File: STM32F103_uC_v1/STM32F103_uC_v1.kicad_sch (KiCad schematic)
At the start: 1 part

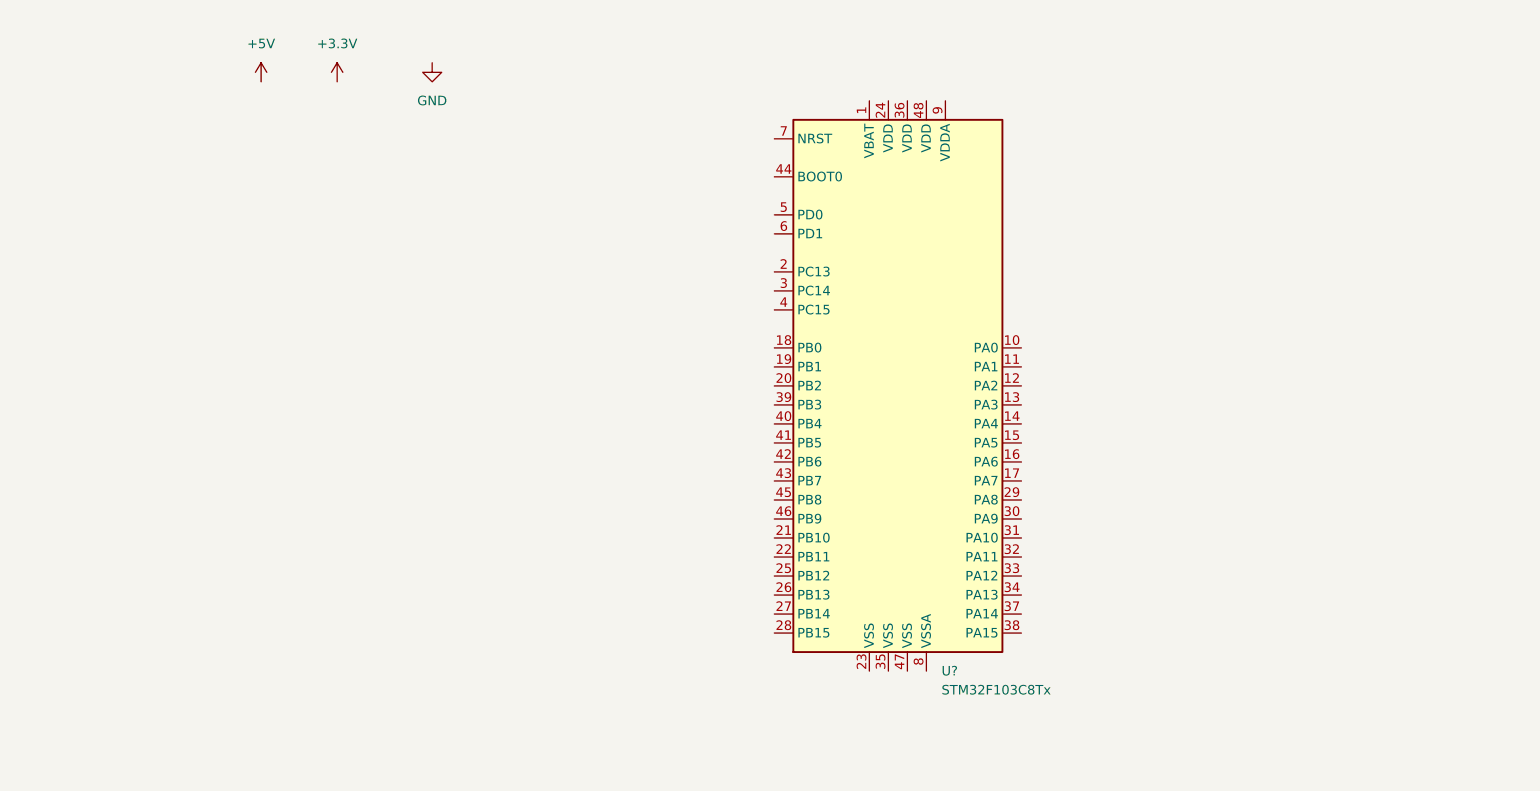
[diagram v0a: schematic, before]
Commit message: 100nF -> 10nF
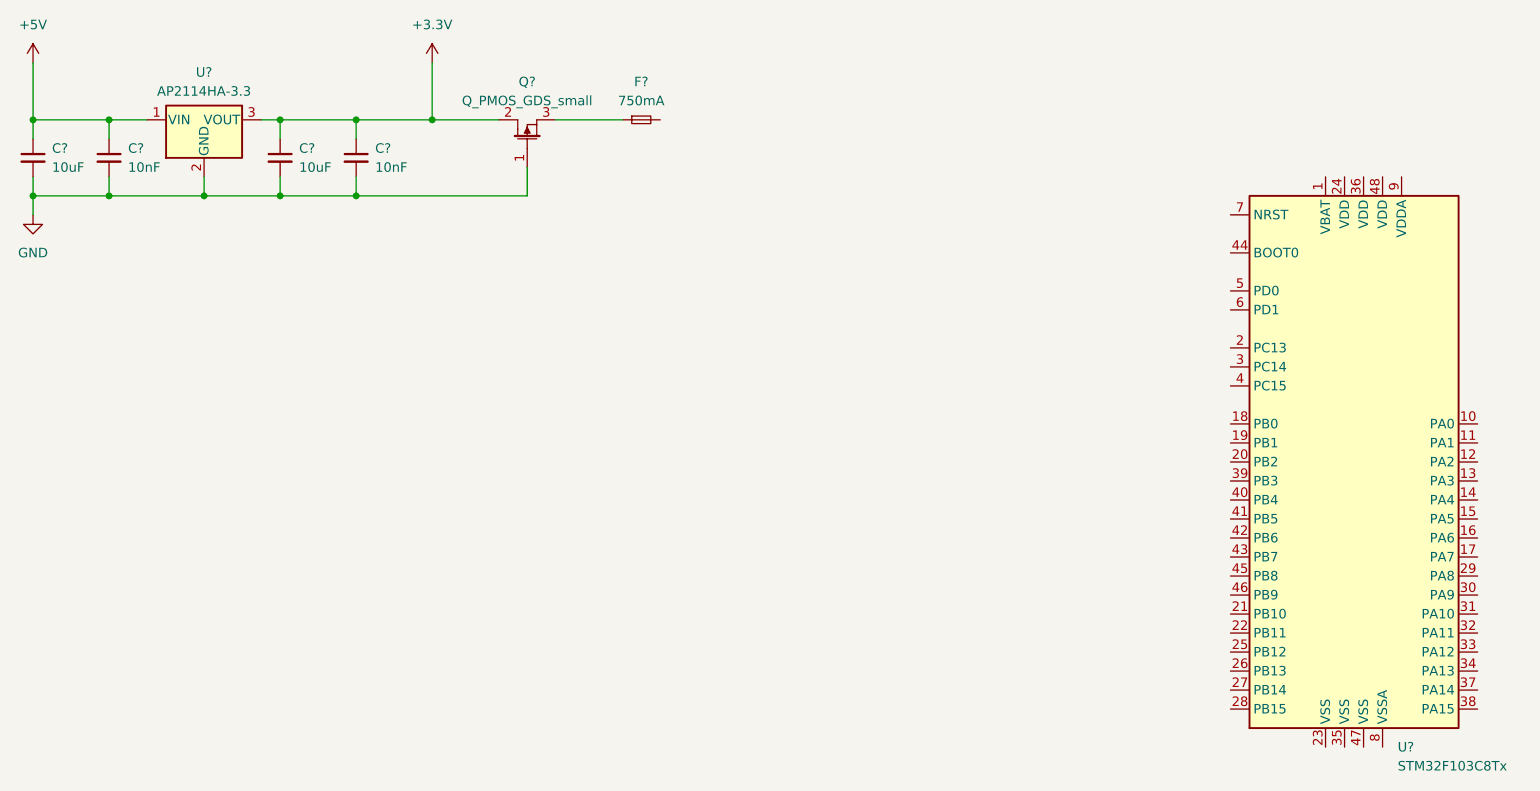
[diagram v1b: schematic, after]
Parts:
- added C? (x2): 10uF, symbol Device:C_Small
- added C? (x2): 10nF, symbol Device:C_Small
- added F?: 750mA, symbol Device:Fuse_Small
- added Q?: Q_PMOS_GDS_small, symbol STM32F103_uC:Q_PMOS_GDS_small
- added U?: AP2114HA-3.3, Package_TO_SOT_SMD:SOT-223-3_TabPin2, symbol STM32F103_uC:AP2114HA-3.3TRG1
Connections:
- net +3V3: now also C?.1, C?.1, Q?.2, U?.3 (VOUT)
- net +5V: now also C?.1, C?.1, U?.1 (VIN)
- net GND: now also C?.2, C?.2, C?.2, C?.2, Q?.1, U?.2 (GND)
- new net: F?.1, Q?.3
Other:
- moved on the sheet: U?

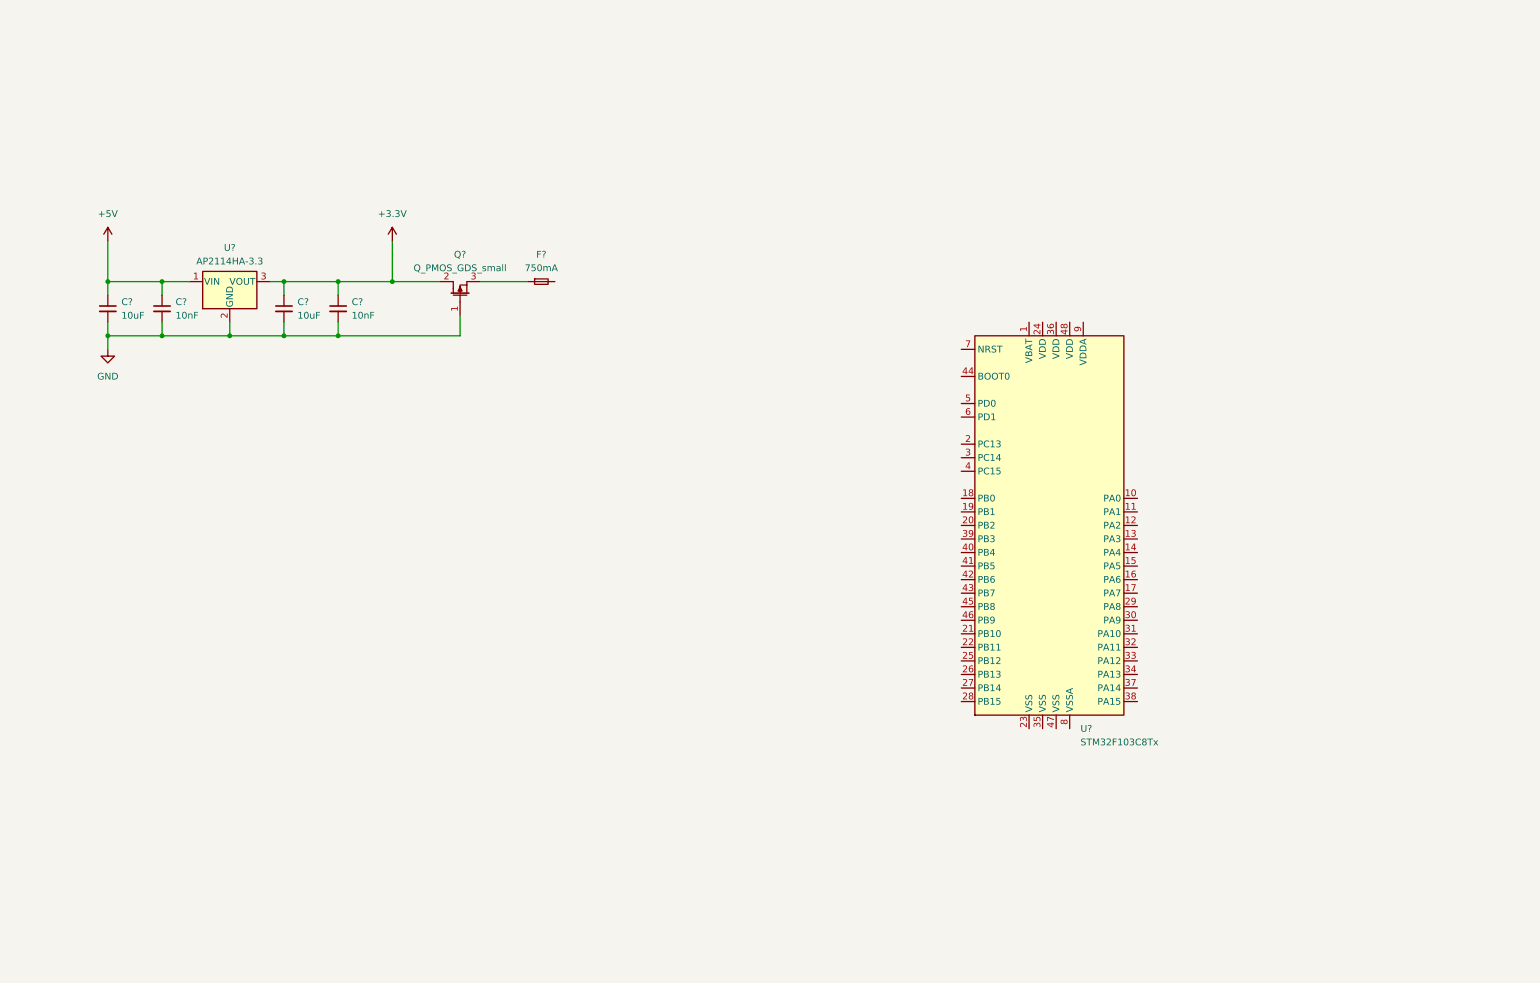
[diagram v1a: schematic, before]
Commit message: Schematic additions
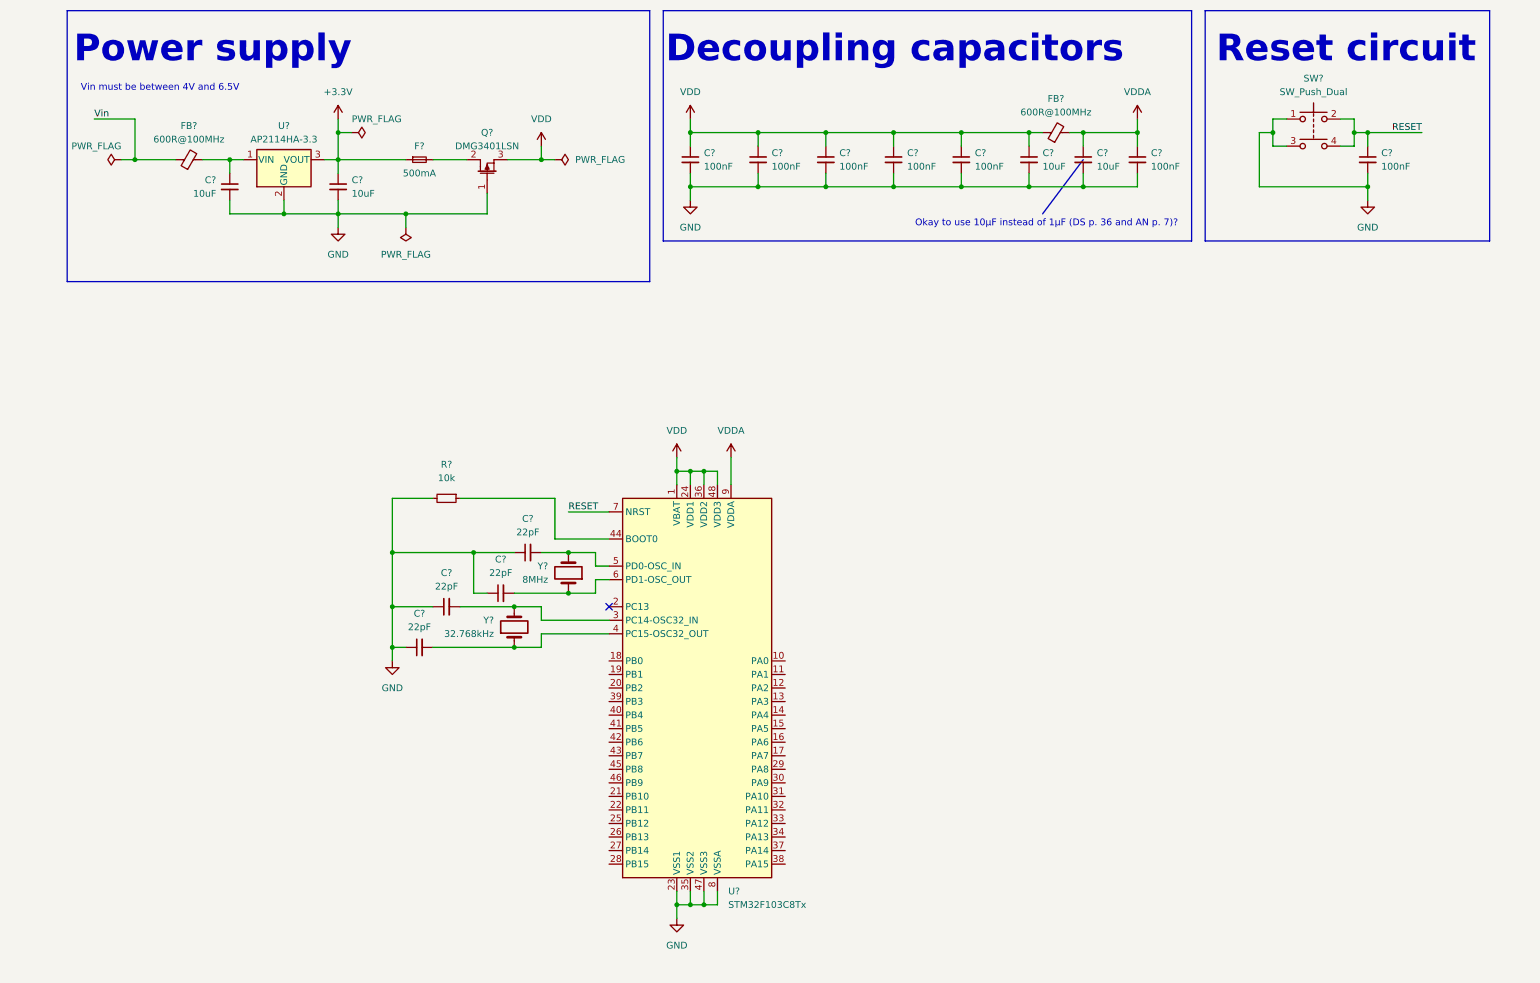
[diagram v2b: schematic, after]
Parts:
- removed C? (x2): 10nF, symbol Device:C_Small
- removed U?: STM32F103C8Tx, Package_QFP:LQFP-48_7x7mm_P0.5mm, symbol MCU_ST_STM32F1:STM32F103C8Tx
- added C? (x7): 100nF, symbol Device:C_Small
- added C? (x4): 22pF, symbol Device:C_Small
- added C? (x2): 10uF, symbol Device:C_Small
- added FB? (x2): 600R@100MHz, symbol Device:FerriteBead_Small
- added R?: 10k, symbol Device:R_Small
- added SW?: SW_Push_Dual, symbol Switch:SW_Push_Dual
- added U?: STM32F103C8Tx, Package_QFP:LQFP-48_7x7mm_P0.5mm, symbol STM32F103_uC:STM32F103C8Tx
- added Y?: 32.768kHz, symbol Device:Crystal
- added Y?: 8MHz, symbol Device:Crystal
- F?: value 750mA -> 500mA
- Q?: value Q_PMOS_GDS_small -> DMG3401LSN
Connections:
- net +3V3: now also F?.1; no longer Q?.2
- net GND: now also C?.1, C?.1, C?.1, C?.1, C?.2, C?.2, C?.2, C?.2, C?.2, C?.2, C?.2, C?.2, C?.2, R?.2, SW?.1, SW?.3, U?.23 (VSS1), U?.35 (VSS2), U?.47 (VSS3), U?.8 (VSSA)
- net VDD: now reaches Q?.3
- net VDD: now also C?.1, C?.1, C?.1, C?.1, C?.1, C?.1, FB?.1, U?.1 (VBAT), U?.24 (VDD1), U?.36 (VDD2), U?.48 (VDD3); no longer F?.1
- net at F?.2: now also Q?.2
- net +5V: no longer names the net of C?.1, U?.1 (VIN)
- net +5V: now also FB?.2
- new net: R?.1, U?.44 (BOOT0)
- new net: C?.2, U?.6 (PD1-OSC_OUT), Y?.1
- new net: C?.2, U?.4 (PC15-OSC32_OUT), Y?.1
- new net: C?.2, U?.3 (PC14-OSC32_IN), Y?.2
- new net: C?.2, U?.5 (PD0-OSC_IN), Y?.2
- new net RESET: C?.1, SW?.2, SW?.4, U?.7 (NRST)
- new net VDDA: C?.1, C?.1, FB?.2, U?.9 (VDDA)
- new net Vin: FB?.1
- no-connect marks 0 -> 1
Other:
- note added: "Decoupling capacitors"
- note added: "Okay to use 10µF instead of 1µF (DS p. 36 and AN p. 7)?"
- note added: "Power supply"
- note added: "Reset circuit"
- note added: "Vin must be between 4V and 6.5V"
- moved on the sheet: C?, F?, Q?, U?

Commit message: cleanup
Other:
- note added: "Microcontroller"
- moved on the sheet: C?, R?, U?, Y?

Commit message: Version 1.0
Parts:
- removed C?: 100nF, symbol Device:C_Small
- added C16: 10µ, Capacitor_SMD:C_0805_2012Metric_Pad1.18x1.45mm_HandSolder, symbol Device:C_Small
- added C17: 100n, Capacitor_SMD:C_0805_2012Metric_Pad1.18x1.45mm_HandSolder, symbol Device:C_Small
- added D2: Green, LED_SMD:LED_1206_3216Metric_Pad1.42x1.75mm_HandSolder, symbol Device:LED_Small
- added H1, H2, H3: MountingHole, MountingHole:MountingHole_3.2mm_M3, symbol Mechanical:MountingHole
- added J1: USB_C_Receptacle, STM32F103_uC:USB_C_Receptacle_GCT_USB4085, symbol Connector:USB_C_Receptacle_USB2.0
- added J2: Barrel_Jack, STM32F103_uC:BarrelJack_Horizontal, symbol Connector:Barrel_Jack_Switch
- added J3, J4: Conn_01x20, Connector_PinHeader_2.54mm:PinHeader_1x20_P2.54mm_Vertical, symbol Connector_Generic:Conn_01x20
- added J5: Screw terminal, TerminalBlock_Phoenix:TerminalBlock_Phoenix_MPT-0,5-2-2.54_1x02_P2.54mm_Horizontal, symbol Connector_Generic:Conn_01x02
- added J6: Conn_01x04, STM32F103_uC:1.3_inch_OLED_IIC, symbol Connector_Generic:Conn_01x04
- added J7: ST-Link V2, STM32F103_uC:PinSocket_2x05_P2.54mm_Vertical, symbol Connector_Generic:Conn_02x05_Odd_Even
- added R10, R7, R8, R9: 2k2, Resistor_SMD:R_0805_2012Metric_Pad1.20x1.40mm_HandSolder, symbol Device:R_Small
- added R11, R12, R13: 10k, Resistor_SMD:R_0805_2012Metric_Pad1.20x1.40mm_HandSolder, symbol Device:R_Small
- added R14, R3: 1k5, Resistor_SMD:R_0805_2012Metric_Pad1.20x1.40mm_HandSolder, symbol Device:R_Small
- added R5: 750R, Resistor_SMD:R_0805_2012Metric_Pad1.20x1.40mm_HandSolder, symbol Device:R_Small
- added R6: 390k, Resistor_SMD:R_0805_2012Metric_Pad1.20x1.40mm_HandSolder, symbol Device:R_Small
- added TC1: Screw terminal, TerminalBlock_Phoenix:TerminalBlock_Phoenix_MPT-0,5-2-2.54_1x02_P2.54mm_Horizontal, symbol Device:Thermocouple
- added U3: MAX31855, Package_SO:SOIC-8_3.9x4.9mm_P1.27mm, symbol STM32F103_uC:MAX31855
- C1, C12, C2: renamed from C?; value 10uF -> 10µ; footprint (none) -> Capacitor_SMD:C_0805_2012Metric_Pad1.18x1.45mm_HandSolder
- C10, C11, C13, C7, C8, C9: renamed from C?; value 100nF -> 100n; footprint (none) -> Capacitor_SMD:C_0805_2012Metric_Pad1.18x1.45mm_HandSolder
- C14: renamed from C?; value 10uF -> 1µ; footprint (none) -> Capacitor_SMD:C_0805_2012Metric_Pad1.18x1.45mm_HandSolder
- C3, C4: renamed from C?; value 22pF -> 27p; footprint (none) -> Capacitor_SMD:C_0805_2012Metric_Pad1.18x1.45mm_HandSolder
- C5, C6: renamed from C?; value 22pF -> 4p; footprint (none) -> Capacitor_SMD:C_0805_2012Metric_Pad1.18x1.45mm_HandSolder
- F1: renamed from F?; value 500mA -> 250; footprint (none) -> Fuse:Fuse_1206_3216Metric_Pad1.42x1.75mm_HandSolder
- FB1, FB2: renamed from FB?; footprint (none) -> Inductor_SMD:L_0805_2012Metric_Pad1.15x1.40mm_HandSolder
- Q1: renamed from Q?; value DMG3401LSN -> DMP2120U-7; footprint (none) -> Package_TO_SOT_SMD:SC-59_Handsoldering
- R4: renamed from R?; footprint (none) -> Resistor_SMD:R_0805_2012Metric_Pad1.20x1.40mm_HandSolder
- SW1: renamed from SW?; footprint (none) -> STM32F103_uC:SW_Push_1P1T_NO_CK_KSC6xxJ
- U1: renamed from U?; value AP2114HA-3.3 -> NCP1117LPST33
- Y1: renamed from Y?; footprint (none) -> STM32F103_uC:Crystal_SMD_Abracon_ABM3-2Pin_5.0x3.2mm_HandSoldering
- Y2: renamed from Y?; footprint (none) -> STM32F103_uC:Crystal_SMD_MicroCrystal_CC7V-T1A-2Pin_3.2x1.5mm_HandSoldering
- gave numbers to parts that had none: 1
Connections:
- net +3V3: now also J4.19 (Pin_19)
- net GND: now also C16.2, D2.1 (K), J1.A1 (GND), J1.A12 (GND), J1.B1 (GND), J1.B12 (GND), J2.2, J2.3, J3.1 (Pin_1), J3.12 (Pin_12), J4.1 (Pin_1), J5.1 (Pin_1), J6.2 (Pin_2), J7.3 (Pin_3), J7.4 (Pin_4), U3.1 (GND)
- net VDD: now also C16.1, J3.11 (Pin_11), J4.2 (Pin_2), J6.1 (Pin_1), J7.7 (Pin_7), J7.8 (Pin_8), R10.1, R11.1, R12.1, R13.1, R14.2, R3.1, R7.1, R8.1, R9.1, U3.4 (VCC); no longer C13.1
- net VDDA: now also C13.1, J4.18 (Pin_18)
- net Vin: now also J1.A4 (VBUS), J1.A9 (VBUS), J1.B4 (VBUS), J1.B9 (VBUS), J2.1, J4.20 (Pin_20)
- net at C4.2, Y1.1: now also R5.1; no longer U2.6 (PD1-OSC_OUT)
- net at C6.2, Y2.1: now also R6.1; no longer U2.4 (PC15-OSC32_OUT)
- net PA0: now reaches U2.10 (PA0)
- net PA0: now also J3.2 (Pin_2)
- net PA1: now reaches U2.11 (PA1)
- net PA1: now also J3.3 (Pin_3)
- net PA2/TX2: now reaches U2.12 (PA2)
- net PA2/TX2: now also J3.4 (Pin_4)
- net PA3/RX2: now reaches U2.13 (PA3)
- net PA3/RX2: now also J3.5 (Pin_5)
- net PA4: now reaches U2.14 (PA4)
- net PA4: now also J3.6 (Pin_6)
- net PA5/SCK1: now reaches U2.15 (PA5)
- net PA5/SCK1: now also J3.7 (Pin_7)
- net PA6/MISO1: now reaches U2.16 (PA6)
- net PA6/MISO1: now also J3.8 (Pin_8)
- net PA7/MOSI1: now reaches U2.17 (PA7)
- net PA7/MOSI1: now also J3.9 (Pin_9)
- net PB0: now reaches U2.18 (PB0)
- net PB0: now also J3.10 (Pin_10)
- net PB1: now reaches U2.19 (PB1)
- net PB1: now also J3.13 (Pin_13)
- net PB2: now reaches U2.20 (PB2)
- net PB2: now also J3.14 (Pin_14), J5.2 (Pin_2)
- net PB10/SCL2: now reaches U2.21 (PB10)
- net PB10/SCL2: now also J3.16 (Pin_16), J6.3 (Pin_3), R9.2
- net PB11/SDA2: now reaches U2.22 (PB11)
- net PB11/SDA2: now also J3.15 (Pin_15), J6.4 (Pin_4), R10.2
- net PB12: now reaches U2.25 (PB12)
- net PB12: now also J3.17 (Pin_17), R13.2, U3.6 (~CS)
- net PB13/SCK2: now reaches U2.26 (PB13)
- net PB13/SCK2: now also J3.18 (Pin_18), R11.2, U3.5 (SCK)
- net PB14/MISO2: now reaches U2.27 (PB14)
- net PB14/MISO2: now also J3.19 (Pin_19), R12.2, U3.7 (SO)
- net PB15/MOSI2: now reaches U2.28 (PB15)
- net PB15/MOSI2: now also J3.20 (Pin_20)
- net PA8: now reaches U2.29 (PA8)
- net PA8: now also J4.3 (Pin_3)
- net PA9/TX1: now reaches U2.30 (PA9)
- net PA9/TX1: now also J4.4 (Pin_4)
- net PA10/RX1: now reaches U2.31 (PA10)
- net PA10/RX1: now also J4.5 (Pin_5)
- net PA11/D-: now reaches U2.32 (PA11)
- net PA11/D-: now also J1.A7 (D-), J1.B7 (D-), J4.6 (Pin_6)
- net PA12/D+: now reaches U2.33 (PA12)
- net PA12/D+: now also J1.A6 (D+), J1.B6 (D+), J4.7 (Pin_7), R14.1
- net PA13/SWDIO: now reaches U2.34 (PA13)
- net PA13/SWDIO: now also J4.8 (Pin_8), J7.2 (Pin_2)
- net PA14/SWCLK: now reaches U2.37 (PA14)
- net PA14/SWCLK: now also J4.9 (Pin_9), J7.6 (Pin_6)
- net PA15: now reaches U2.38 (PA15)
- net PA15: now also J4.10 (Pin_10)
- net PB3/SWO: now reaches U2.39 (PB3)
- net PB3/SWO: now also J4.11 (Pin_11), J7.5 (Pin_5)
- net PB4: now reaches U2.40 (PB4)
- net PB4: now also J4.12 (Pin_12)
- net PB5: now reaches U2.41 (PB5)
- net PB5: now also J4.13 (Pin_13)
- net PB6/SCL1: now reaches U2.42 (PB6)
- net PB6/SCL1: now also J4.14 (Pin_14), R7.2
- net PB7/SDA1: now reaches U2.43 (PB7)
- net PB7/SDA1: now also J4.15 (Pin_15), R8.2
- net PB8: now reaches U2.45 (PB8)
- net PB8: now also J4.16 (Pin_16)
- net PB9: now reaches U2.46 (PB9)
- net PB9: now also J4.17 (Pin_17)
- net RESET renamed ~RST
- net ~RST: now also J7.1 (Pin_1)
- new net: R6.2, U2.4 (PC15-OSC32_OUT)
- new net: R5.2, U2.6 (PD1-OSC_OUT)
- new net: C17.1, TC1.1 (+), U3.3 (T+)
- new net: C17.2, TC1.2 (-), U3.2 (T-)
- new net: D2.2 (A), R3.2
- no-connect marks 1 -> 8
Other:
- note added: "MCU power conditioning"
- note added: "Mounting holes"
- note added: "OLED"
- note added: "Pin headers"
- note added: "Relay"
- note added: "Serial wire debugger"
- note added: "Thermocouple"
- note added: "Vin must be between 4.5V and 18V"
- note removed: "Decoupling capacitors"
- note removed: "Okay to use 10µF instead of 1µF (DS p. 36 and AN p. 7)?"
- note removed: "Vin must be between 4V and 6.5V"
- moved on the sheet: C1, C10, C11, C12, C13, C14, C2, C3, C4, C5, C6, C7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

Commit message: Finishing touches
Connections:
- net PA11/D- renamed USB_D-
- net PA12/D+ renamed USB_D+
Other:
- company: (none) -> IL2237 Electronic Systems Design
- title: (none) -> Hot-Plate Reflow Controller
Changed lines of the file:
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@@
 (kicad_sch (version 20211123) (generator eeschema)
   (paper "A4")
+  (title_block
+    (title "Hot-Plate Reflow Controller")
+    (date "08/04/2022")
+    (rev "1.0")
+    (company "IL2237 Electronic Systems Design")
+    (comment 1 "Egill Milan Gunnarsson")
+  )
   (junction (at 213.36 86.36) (diameter 0) (color 0 0 0 0)
   )
@@
     (effects (font (size 1.27 1.27)) (justify right bottom))
   )
-  (label "PA12{slash}D+" (at 119.38 152.4 0)
+  (label "USB_D+" (at 119.38 152.4 0)
     (effects (font (size 1.27 1.27)) (justify left bottom))
   )
@@
     (effects (font (size 1.27 1.27)) (justify left bottom))
   )
-  (label "PA11{slash}D-" (at 279.4 134.62 180)
+  (label "USB_D-" (at 279.4 134.62 180)
     (effects (font (size 1.27 1.27)) (justify right bottom))
   )
@@
     (effects (font (size 1.27 1.27)) (justify left bottom))
   )
-  (label "PA11{slash}D-" (at 119.38 149.86 0)
+  (label "USB_D-" (at 119.38 149.86 0)
     (effects (font (size 1.27 1.27)) (justify left bottom))
   )
@@
     (effects (font (size 1.27 1.27)) (justify right bottom))
   )
-  (label "PA11{slash}D-" (at 63.5 38.1 180)
-    (effects (font (size 1.27 1.27)) (justify right bottom))
-  )
-  (label "PA12{slash}D+" (at 63.5 43.18 180)
+  (label "USB_D-" (at 63.5 38.1 180)
+    (effects (font (size 1.27 1.27)) (justify right bottom))
+  )
+  (label "USB_D+" (at 63.5 43.18 180)
     (effects (font (size 1.27 1.27)) (justify right bottom))
   )
@@
     (effects (font (size 1.27 1.27)) (justify left bottom))
   )
-  (label "PA12{slash}D+" (at 279.4 137.16 180)
+  (label "USB_D+" (at 279.4 137.16 180)
     (effects (font (size 1.27 1.27)) (justify right bottom))
   )
@@
       (effects (font (size 1.27 1.27)) (justify right))
     )
-    (property "Value" "Screw terminal" (id 1) (at 55.88 140.97 0)
+    (property "Value" "Screw terminal" (id 1) (at 55.88 139.7 0)
       (effects (font (size 1.27 1.27)) (justify right))
     )
